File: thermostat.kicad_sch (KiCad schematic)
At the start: 92 parts, among them U17 AD5680, U18 AD7172-2, U19 RS8552, U20 MAX1968xUI, U29 AD7172-4BCPZ

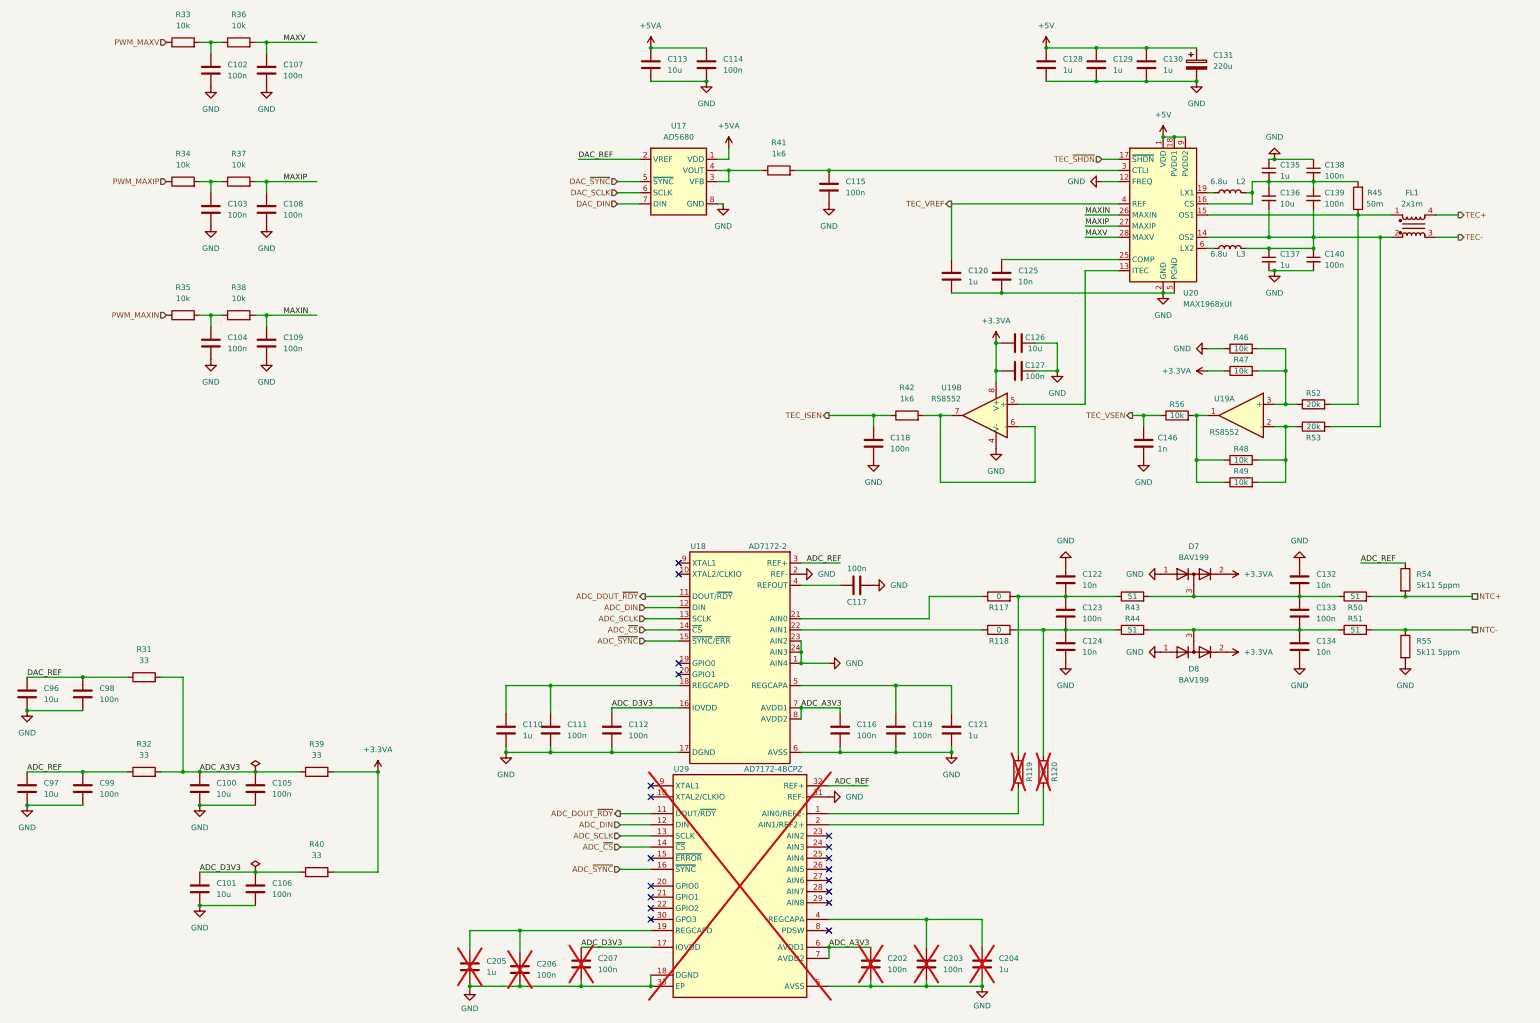
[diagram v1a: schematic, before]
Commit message: pcb: Finish Layout for rev0_3 - Assign MFR_PN for all Components - schematics changes:   - drivestage: Add Switch to optionally enable Modulation Signal Termination   -             Add alternate Precision Power Resistor   -             Modify the RC network values at TIA LPF Output   - MCU: Add Redundant 2.54mm pitch Programming Header   - thermostat: Duplicate the power filter network for alternate Temperature ADC
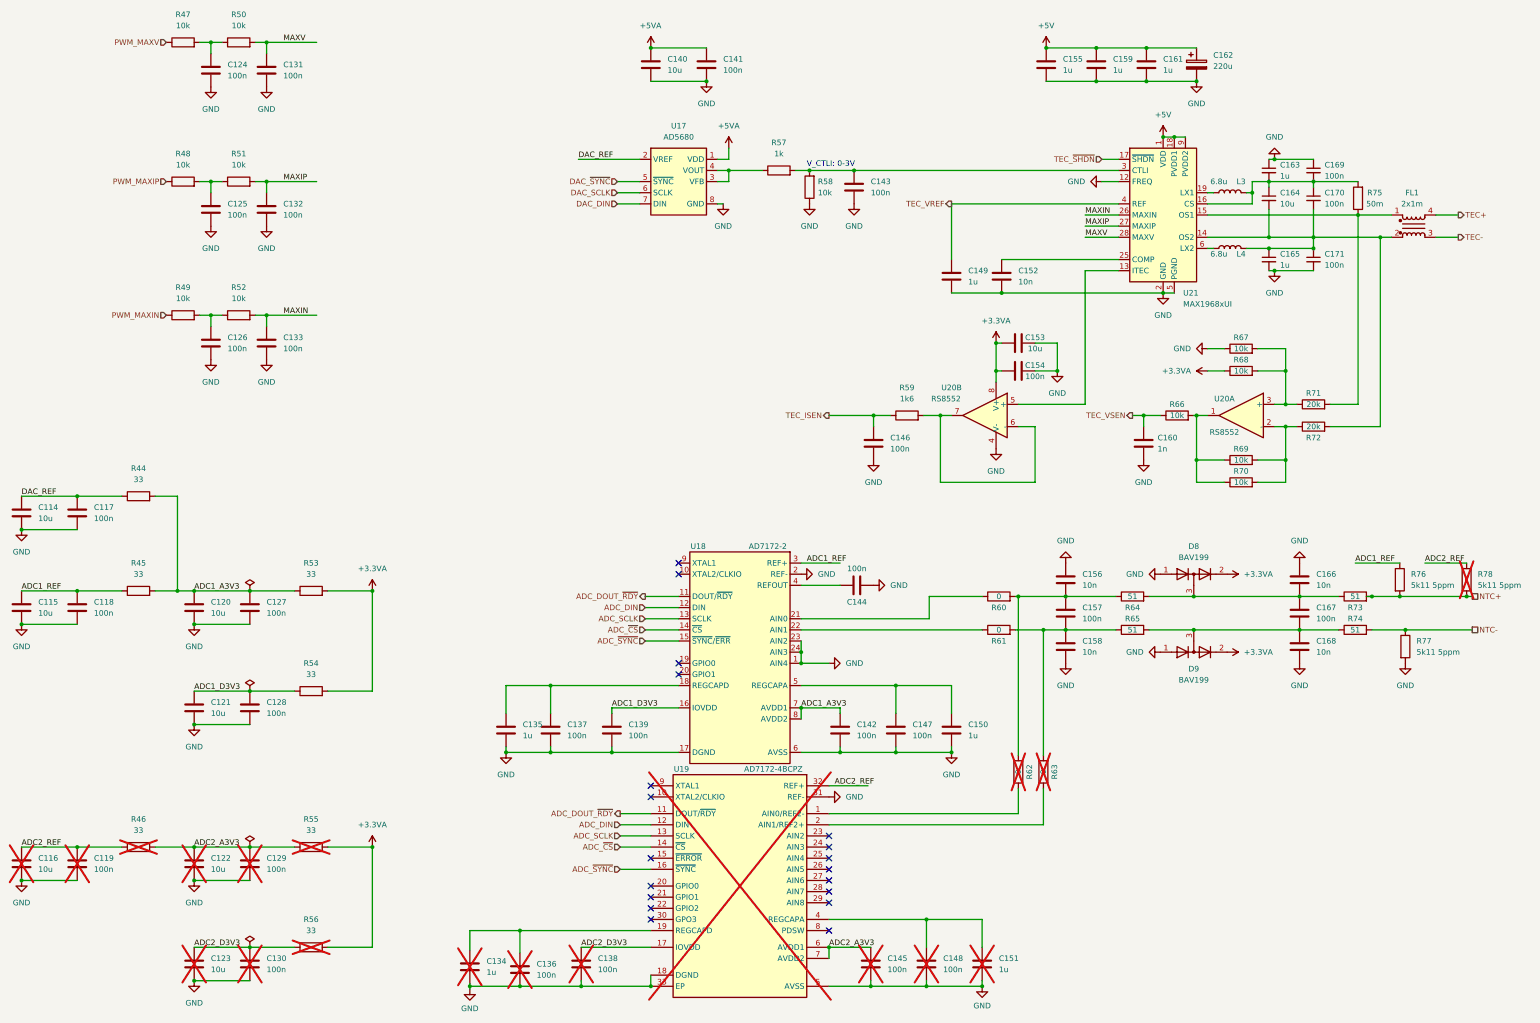
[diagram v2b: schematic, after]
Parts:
- added C116, C122, C123: 10u, Capacitor_SMD:C_0805_2012Metric, symbol Device:C
- added C119, C129, C130: 100n, Capacitor_SMD:C_0603_1608Metric, symbol Device:C
- added R46, R55, R56: 33, Resistor_SMD:R_0603_1608Metric, symbol Device:R
- added R58: 10k, Resistor_SMD:R_0603_1608Metric, symbol Device:R
- added R78: 5k11 5ppm, Resistor_SMD:R_0603_1608Metric, symbol Device:R
- C160: renamed from C146; MFR_PN (none) -> 0603N102G250CT; MFR_PN_ALT CL10B104KB8NNNL -> (none)
- R57: renamed from R41; value 1k6 -> 1k; MFR_PN RT0603FRE071K6L -> RP0603BRD071KL; MFR_PN_ALT RMCF0603FT1K60 -> WR06X1001FTL
- R60: renamed from R117; MFR_PN (none) -> RMCF0603ZT0R00; MFR_PN_ALT RMCF0603FT51R0 -> CR0603-J/-000ELF
- R61: renamed from R118; MFR_PN (none) -> RMCF0603ZT0R00; MFR_PN_ALT RMCF0603FT51R0 -> CR0603-J/-000ELF
- R62: renamed from R119; MFR_PN (none) -> RMCF0603ZT0R00; MFR_PN_ALT RMCF0603FT51R0 -> CR0603-J/-000ELF
- R63: renamed from R120; MFR_PN (none) -> RMCF0603ZT0R00; MFR_PN_ALT RMCF0603FT51R0 -> CR0603-J/-000ELF
- U19: renamed from U29; Height 0.8 -> (none); MFR_PN (none) -> AD7172-4BCPZ; MF_PN AD7172-4BCPZ -> (none); Manufacturer_Name Analog Devices -> (none); Mouser Part Number 584-AD7172-4BCPZ -> (none); Mouser Price/Stock https://www.mouser.co.uk/ProductDetail/Analog-Devices/AD717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 -> (none)
- U21: renamed from U20; MFR_PN (none) -> MAX1968EUI+T
- renumbered C96 to C114, C97 to C115, C98 to C117, C99 to C118, C100 to C120, C101 to C121, C102 to C124, C103 to C125, C104 to C126, C105 to C127, C106 to C128, C107 to C131, C108 to C132, C109 to C133, C205 to C134, C110 to C135, C206 to C136, C111 to C137, C207 to C138, C112 to C139, C113 to C140, C114 to C141, C116 to C142, C115 to C143, C117 to C144, C202 to C145, C118 to C146, C119 to C147, C203 to C148, C120 to C149, C121 to C150, C204 to C151, C125 to C152, C126 to C153, C127 to C154, C128 to C155, C122 to C156, C123 to C157, C124 to C158, C129 to C159, C130 to C161, C131 to C162, C135 to C163, C136 to C164, C137 to C165, C132 to C166, C133 to C167, C134 to C168, C138 to C169, C139 to C170, C140 to C171, D7 to D8, D8 to D9, L2 to L3, L3 to L4, R31 to R44, R32 to R45, R33 to R47, R34 to R48, R35 to R49, R36 to R50, R37 to R51, R38 to R52, R39 to R53, R40 to R54, R42 to R59, R43 to R64, R44 to R65, R56 to R66, R46 to R67, R47 to R68, R48 to R69, R49 to R70, R52 to R71, R53 to R72, R50 to R73, R51 to R74, R45 to R75, R54 to R76, R55 to R77, U19 to U20
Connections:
- net +3.3VA: now also R55.2, R56.2
- net GND: now also C116.2, C119.2, C122.2, C123.2, C129.2, C130.2, R58.1
- net NTC+: now also R78.2
- net at C143.1, R57.2, U21.3 (CTLI): now also R58.2
- net ADC_A3V3 renamed ADC1_A3V3
- net ADC1_A3V3: no longer C145.1, U19.6 (AVDD1), U19.7 (AVDD2)
- net ADC_D3V3 renamed ADC1_D3V3
- net ADC1_D3V3: no longer C138.1, U19.17 (IOVDD)
- net ADC_REF renamed ADC1_REF
- net ADC1_REF: no longer U19.32 (REF+)
- new net ADC2_A3V3: C122.1, C129.1, C145.1, R46.2, R55.1, U19.6 (AVDD1), U19.7 (AVDD2)
- new net ADC2_D3V3: C123.1, C130.1, C138.1, R56.1, U19.17 (IOVDD)
- new net ADC2_REF: C116.1, C119.1, R46.1, R78.1, U19.32 (REF+)
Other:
- note added: "V_CTLI: 0-3V"
- moved on the sheet: C114, C115, C117, C118, C120, C121, C127, C128, C143, R44, R45, R53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

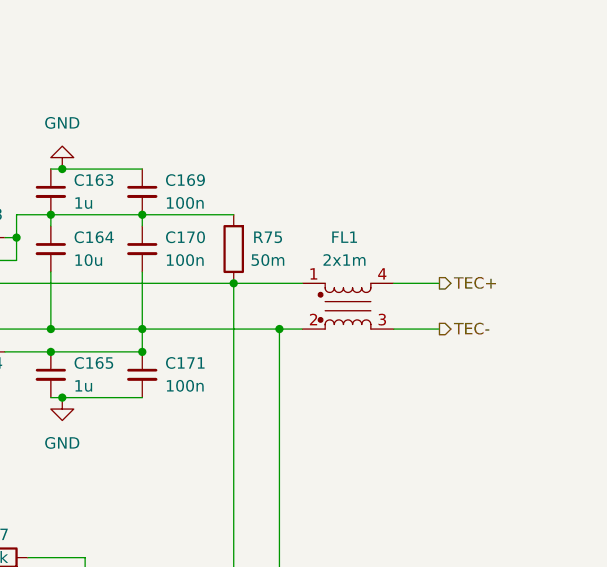
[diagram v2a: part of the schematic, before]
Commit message: thermostat: Fix wrong P/N in TEC Current Sense Res - Fix Issue #26
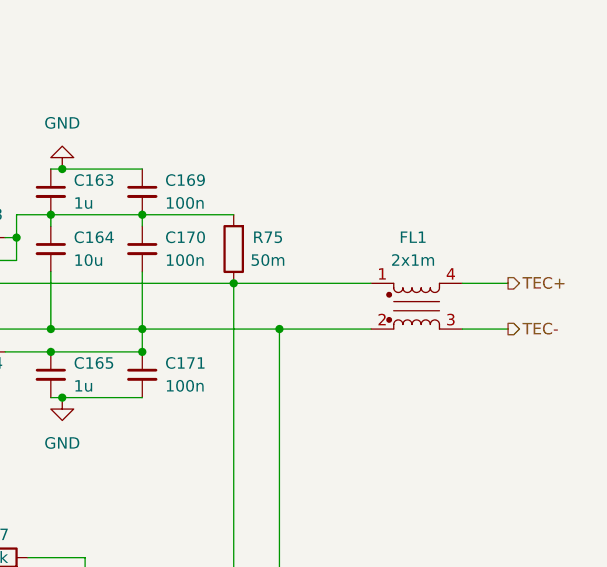
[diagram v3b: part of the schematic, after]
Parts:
- R75: MFR_PN WSL2010R5000FEA18 -> CRM2010-FX-R050ELF
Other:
- moved on the sheet: FL1
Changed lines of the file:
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@@
     (stroke (width 0) (type default))
   )
-  (wire (pts (xy 363.22 101.6) (xy 368.3 101.6))
+  (wire (pts (xy 370.84 101.6) (xy 375.92 101.6))
     (stroke (width 0) (type default))
   )
@@
     (stroke (width 0) (type default))
   )
-  (wire (pts (xy 350.52 106.68) (xy 353.06 106.68))
+  (wire (pts (xy 350.52 106.68) (xy 360.68 106.68))
     (stroke (width 0) (type default))
   )
@@
     (stroke (width 0) (type default))
   )
-  (wire (pts (xy 345.44 101.6) (xy 353.06 101.6))
+  (wire (pts (xy 345.44 101.6) (xy 360.68 101.6))
     (stroke (width 0) (type default))
   )
@@
     (stroke (width 0) (type default))
   )
-  (wire (pts (xy 363.22 106.68) (xy 368.3 106.68))
+  (wire (pts (xy 370.84 106.68) (xy 375.92 106.68))
     (stroke (width 0) (type default))
   )
@@
     (effects (font (size 1.27 1.27)) (justify right))
   )
-  (hierarchical_label "TEC+" (shape output) (at 368.3 101.6 0) (fields_autoplaced)
+  (hierarchical_label "TEC+" (shape output) (at 375.92 101.6 0) (fields_autoplaced)
     (effects (font (size 1.27 1.27)) (justify left))
   )
@@
     (effects (font (size 1.27 1.27)) (justify left))
   )
-  (hierarchical_label "TEC-" (shape output) (at 368.3 106.68 0) (fields_autoplaced)
+  (hierarchical_label "TEC-" (shape output) (at 375.92 106.68 0) (fields_autoplaced)
     (effects (font (size 1.27 1.27)) (justify left))
   )
@@
       (effects (font (size 1.27 1.27)) hide)
     )
-    (property "MFR_PN" "WSL2010R5000FEA18" (at 345.44 97.79 0)
+    (property "MFR_PN" "CRM2010-FX-R050ELF" (at 345.44 97.79 0)
       (effects (font (size 1.27 1.27)) hide)
     )
@@
     )
   )
-  (symbol (lib_id "Device:Filter_EMI_LL_1423") (at 358.14 104.14 0) (mirror x) (unit 1)
-    (in_bom yes) (on_board yes) (dnp no) (fields_autoplaced)
-    (property "Reference" "FL1" (at 357.759 96.52 0)
-      (effects (font (size 1.27 1.27)))
-    )
-    (property "Value" "2x1m" (at 357.759 99.06 0)
-      (effects (font (size 1.27 1.27)))
-    )
-    (property "Footprint" "Inductor_SMD:L_CommonModeChoke_Wuerth_WE-SL5" (at 358.14 97.79 0)
-      (effects (font (size 1.27 1.27)) hide)
-    )
-    (property "Datasheet" "~" (at 358.14 105.156 90)
-      (effects (font (size 1.27 1.27)) hide)
-    )
-    (property "MFR_PN" "744273501" (at 358.14 104.14 0)
-      (effects (font (size 1.27 1.27)) hide)
-    )
+  (symbol (lib_id "Device:Filter_EMI_LL_1423") (at 365.76 104.14 0) (mirror x) (unit 1)
+    (in_bom yes) (on_board yes) (dnp no) (fields_autoplaced)
+    (property "Reference" "FL1" (at 365.379 96.52 0)
+      (effects (font (size 1.27 1.27)))
+    )
+    (property "Value" "2x1m" (at 365.379 99.06 0)
+      (effects (font (size 1.27 1.27)))
+    )
+    (property "Footprint" "Inductor_SMD:L_CommonModeChoke_Wuerth_WE-SL5" (at 365.76 97.79 0)
+      (effects (font (size 1.27 1.27)) hide)
+    )
+    (property "Datasheet" "~" (at 365.76 105.156 90)
+      (effects (font (size 1.27 1.27)) hide)
+    )
+    (property "MFR_PN" "744273501" (at 365.76 104.14 0)
+      (effects (font (size 1.27 1.27)) hide)
+    )
